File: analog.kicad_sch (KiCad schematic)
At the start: 45 parts, among them J8 Sensor harness

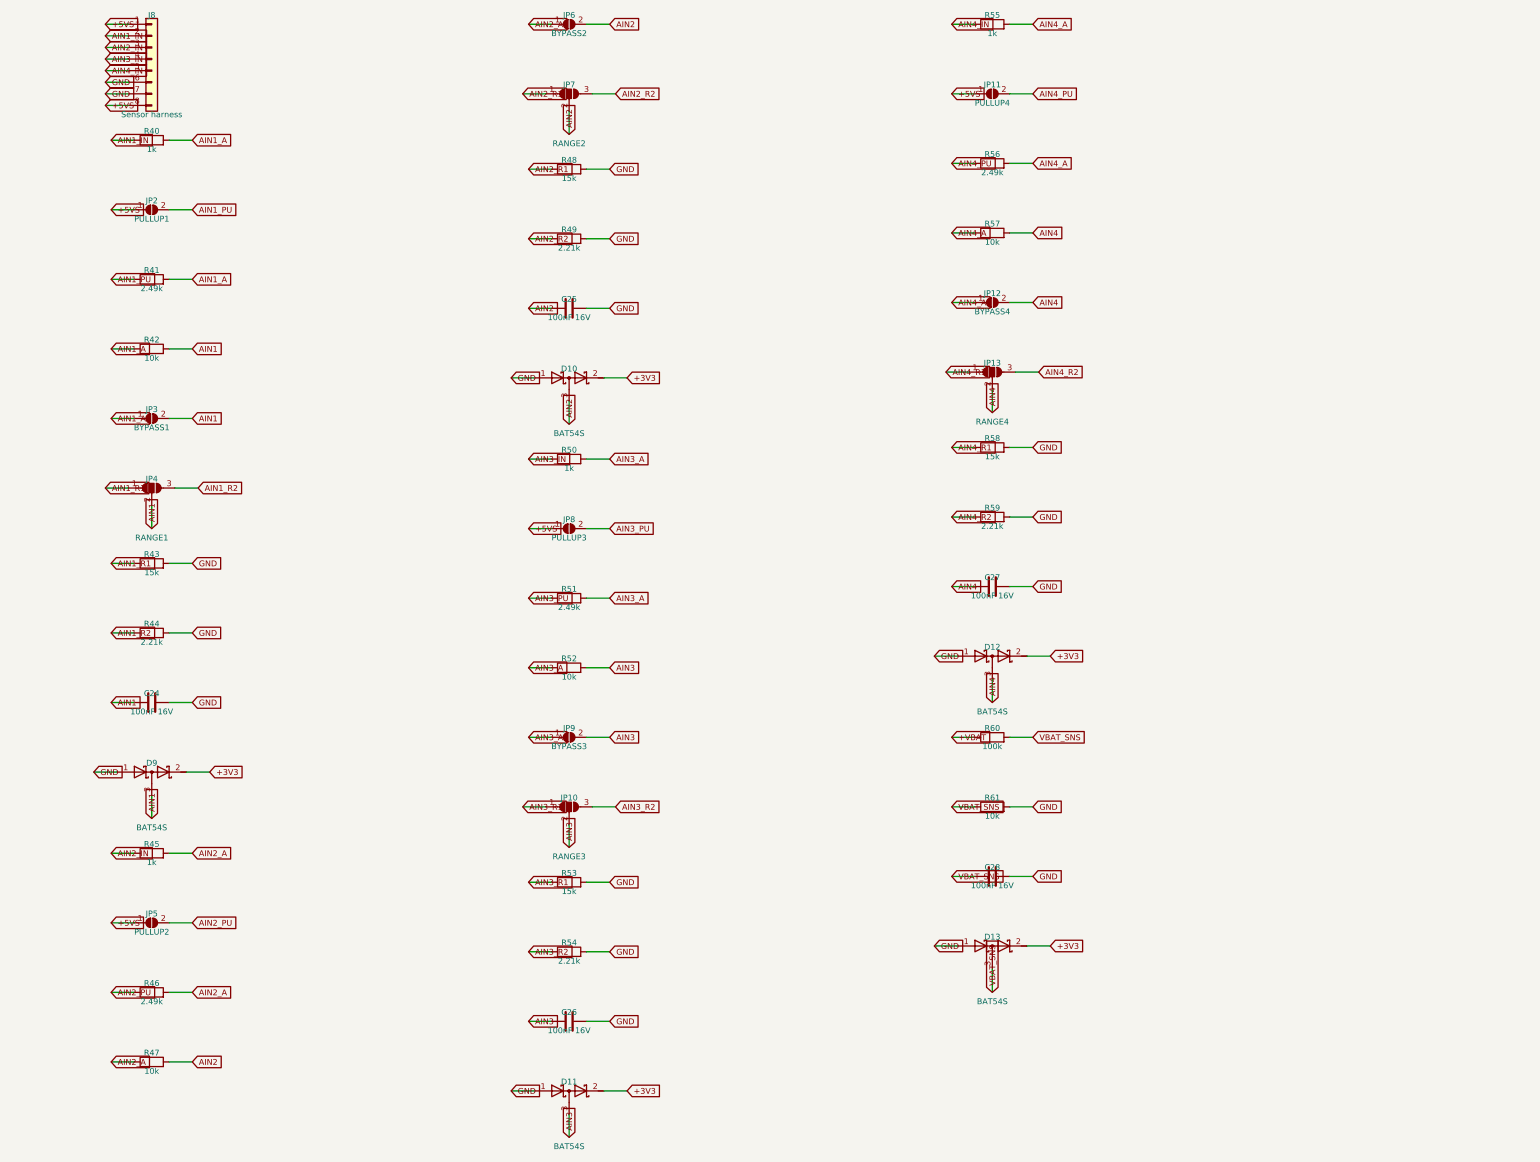
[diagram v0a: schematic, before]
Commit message: Pass ERC clean on KiCad 9.0 and regenerate against its libraries
- Add a PWR_FLAG on VBAT_FB so the LM74700 ANODE power-input pin, fed
  through the reverse-battery FET and EMI bead, no longer trips
  power_pin_not_driven.
- Resolve the generic MOSFET symbols from Transistor_FET where the
  KiCad 9 libraries moved them out of Device.
- Handle the KiCad 9 library format in the raw-symbol extractor: tab
  indentation, CRLF line endings, and no trailing space after the
  symbol name.
- Flatten derived symbols the way KiCad does — carry the child's whole
  property blocks into the parent geometry instead of only swapping the
  value strings — so the embedded USBLC6-2SC6 matches the library copy.
- Regenerate all sheets, netlist, and the PDF plot; embedded symbol
  definitions now come from the KiCad 9.0 (20241209) libraries.

Validated with kicad-cli 9.0: all sheets load, connectivity matches
netlist.txt on 102 nets / 153 instances, ERC clean.

Co-Authored-By: Claude Fable 5 <noreply@anthropic.com>
Claude-Session: https://claude.ai/code/session_01DhNbL25h25p8VFCjRfJik9
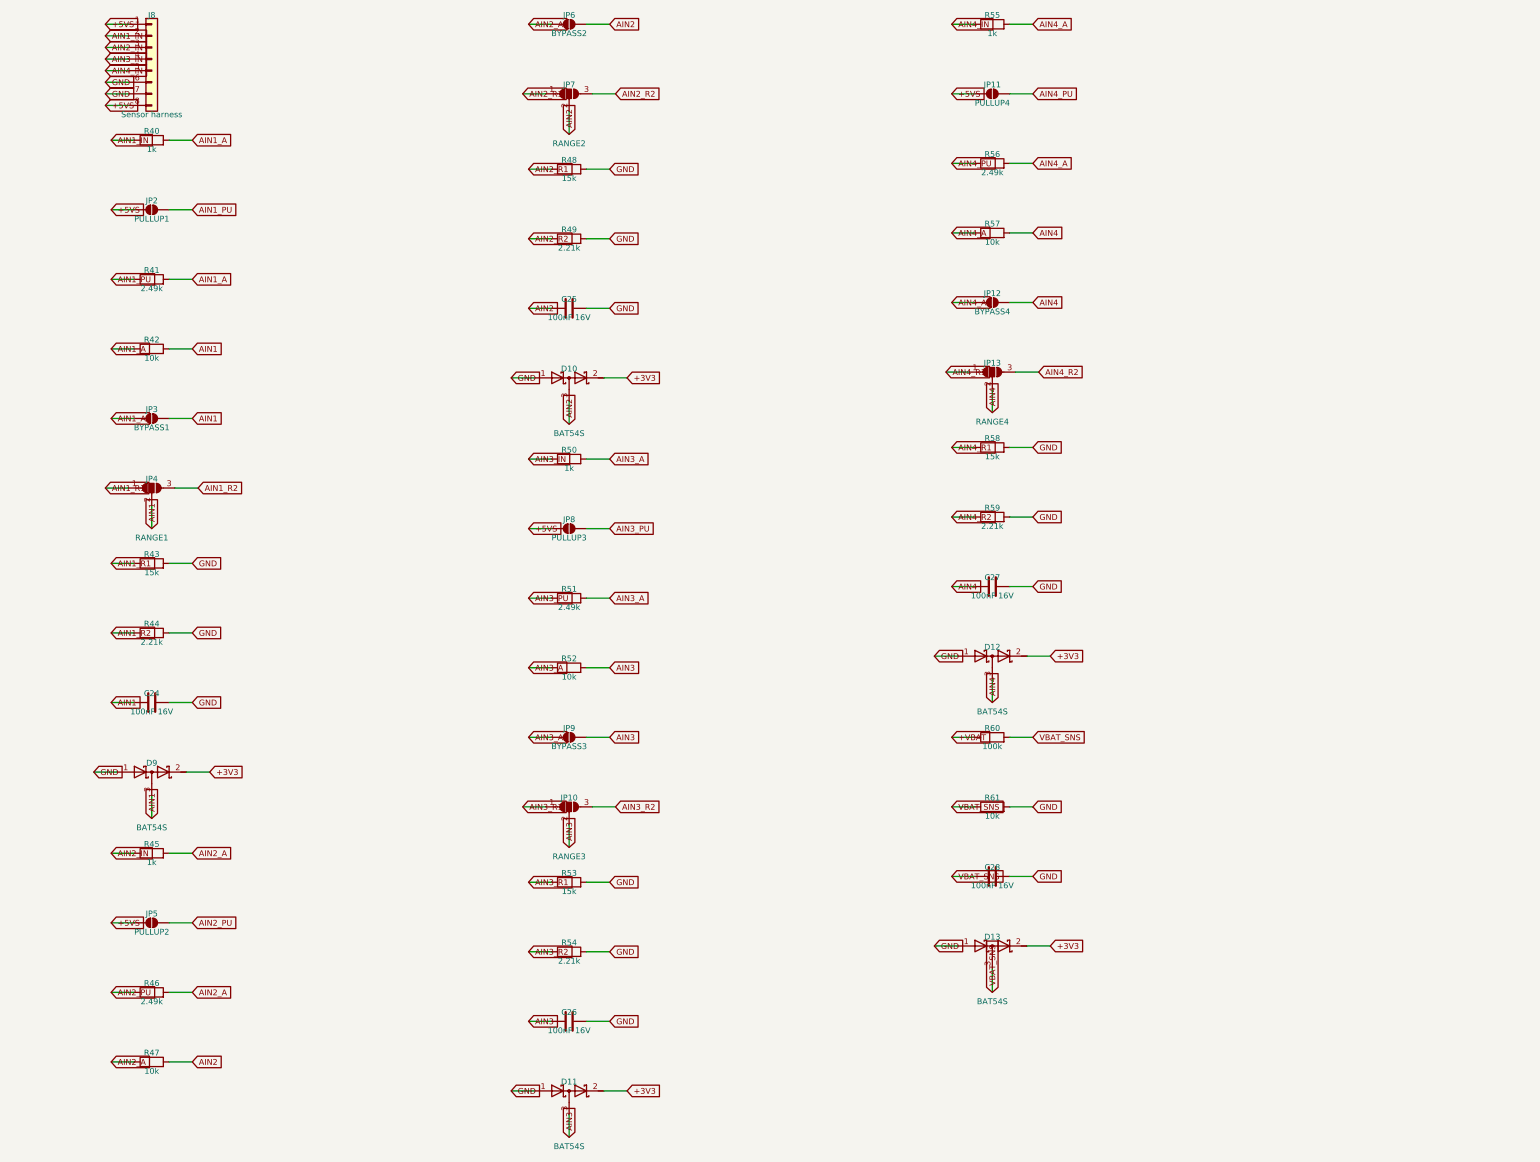
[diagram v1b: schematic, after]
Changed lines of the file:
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@@
+    (stroke (width 0) (type default))
+  )
+  (wire (pts (xy 54.61 186.69) (xy 54.61 191.77))
     (stroke (width 0) (type default))
   )
@@
     (stroke (width 0) (type default))
   )
-  (wire (pts (xy 54.61 186.69) (xy 54.61 191.77))
-    (stroke (width 0) (type default))
-  )
   (wire (pts (xy 50.8 199.39) (xy 45.72 199.39))
     (stroke (width 0) (type default))
@@
     (stroke (width 0) (type default))
   )
+  (wire (pts (xy 146.05 100.33) (xy 146.05 105.41))
+    (stroke (width 0) (type default))
+  )
   (wire (pts (xy 153.67 95.25) (xy 158.75 95.25))
     (stroke (width 0) (type default))
   )
-  (wire (pts (xy 146.05 100.33) (xy 146.05 105.41))
-    (stroke (width 0) (type default))
-  )
   (wire (pts (xy 142.24 113.03) (xy 137.16 113.03))
     (stroke (width 0) (type default))
@@
     (stroke (width 0) (type default))
   )
+  (wire (pts (xy 146.05 256.54) (xy 146.05 261.62))
+    (stroke (width 0) (type default))
+  )
   (wire (pts (xy 153.67 251.46) (xy 158.75 251.46))
     (stroke (width 0) (type default))
   )
-  (wire (pts (xy 146.05 256.54) (xy 146.05 261.62))
-    (stroke (width 0) (type default))
-  )
   (wire (pts (xy 234.95 17.78) (xy 229.87 17.78))
     (stroke (width 0) (type default))
@@
     (stroke (width 0) (type default))
   )
+  (wire (pts (xy 238.76 161.29) (xy 238.76 166.37))
+    (stroke (width 0) (type default))
+  )
   (wire (pts (xy 246.38 156.21) (xy 251.46 156.21))
     (stroke (width 0) (type default))
   )
-  (wire (pts (xy 238.76 161.29) (xy 238.76 166.37))
-    (stroke (width 0) (type default))
-  )
   (wire (pts (xy 234.95 173.99) (xy 229.87 173.99))
     (stroke (width 0) (type default))
@@
     (stroke (width 0) (type default))
   )
+  (wire (pts (xy 238.76 224.79) (xy 238.76 229.87))
+    (stroke (width 0) (type default))
+  )
   (wire (pts (xy 246.38 219.71) (xy 251.46 219.71))
     (stroke (width 0) (type default))
   )
-  (wire (pts (xy 238.76 224.79) (xy 238.76 229.87))
-    (stroke (width 0) (type default))
-  )
   (global_label "+5VS" (shape input) (at 44.45 17.78 180) (fields_autoplaced)
     (effects (font (size 1.27 1.27)) (justify left))
@@
     )
   )
+  (global_label "AIN1" (shape input) (at 54.61 191.77 270) (fields_autoplaced)
+    (effects (font (size 1.27 1.27)) (justify left))
+    (property "Intersheet References" "${INTERSHEET_REFS}" (at 54.61 191.77 0)
+      (effects (font (size 1.27 1.27)) (justify left) hide)
+    )
+  )
   (global_label "+3V3" (shape input) (at 67.31 181.61 0) (fields_autoplaced)
     (effects (font (size 1.27 1.27)) (justify left))
@@
     )
   )
-  (global_label "AIN1" (shape input) (at 54.61 191.77 270) (fields_autoplaced)
-    (effects (font (size 1.27 1.27)) (justify left))
-    (property "Intersheet References" "${INTERSHEET_REFS}" (at 54.61 191.77 0)
-      (effects (font (size 1.27 1.27)) (justify left) hide)
-    )
-  )
   (global_label "AIN2_IN" (shape input) (at 45.72 199.39 180) (fields_autoplaced)
     (effects (font (size 1.27 1.27)) (justify left))
@@
     )
   )
+  (global_label "AIN2" (shape input) (at 146.05 105.41 270) (fields_autoplaced)
+    (effects (font (size 1.27 1.27)) (justify left))
+    (property "Intersheet References" "${INTERSHEET_REFS}" (at 146.05 105.41 0)
+      (effects (font (size 1.27 1.27)) (justify left) hide)
+    )
+  )
   (global_label "+3V3" (shape input) (at 158.75 95.25 0) (fields_autoplaced)
     (effects (font (size 1.27 1.27)) (justify left))
@@
     )
   )
-  (global_label "AIN2" (shape input) (at 146.05 105.41 270) (fields_autoplaced)
-    (effects (font (size 1.27 1.27)) (justify left))
-    (property "Intersheet References" "${INTERSHEET_REFS}" (at 146.05 105.41 0)
-      (effects (font (size 1.27 1.27)) (justify left) hide)
-    )
-  )
   (global_label "AIN3_IN" (shape input) (at 137.16 113.03 180) (fields_autoplaced)
     (effects (font (size 1.27 1.27)) (justify left))
@@
     )
   )
+  (global_label "AIN3" (shape input) (at 146.05 261.62 270) (fields_autoplaced)
+    (effects (font (size 1.27 1.27)) (justify left))
+    (property "Intersheet References" "${INTERSHEET_REFS}" (at 146.05 261.62 0)
+      (effects (font (size 1.27 1.27)) (justify left) hide)
+    )
+  )
   (global_label "+3V3" (shape input) (at 158.75 251.46 0) (fields_autoplaced)
     (effects (font (size 1.27 1.27)) (justify left))
@@
     )
   )
-  (global_label "AIN3" (shape input) (at 146.05 261.62 270) (fields_autoplaced)
-    (effects (font (size 1.27 1.27)) (justify left))
-    (property "Intersheet References" "${INTERSHEET_REFS}" (at 146.05 261.62 0)
-      (effects (font (size 1.27 1.27)) (justify left) hide)
-    )
-  )
   (global_label "AIN4_IN" (shape input) (at 229.87 17.78 180) (fields_autoplaced)
     (effects (font (size 1.27 1.27)) (justify left))
@@
     )
   )
+  (global_label "AIN4" (shape input) (at 238.76 166.37 270) (fields_autoplaced)
+    (effects (font (size 1.27 1.27)) (justify left))
+    (property "Intersheet References" "${INTERSHEET_REFS}" (at 238.76 166.37 0)
+      (effects (font (size 1.27 1.27)) (justify left) hide)
+    )
+  )
   (global_label "+3V3" (shape input) (at 251.46 156.21 0) (fields_autoplaced)
     (effects (font (size 1.27 1.27)) (justify left))
@@
     )
   )
-  (global_label "AIN4" (shape input) (at 238.76 166.37 270) (fields_autoplaced)
-    (effects (font (size 1.27 1.27)) (justify left))
-    (property "Intersheet References" "${INTERSHEET_REFS}" (at 238.76 166.37 0)
-      (effects (font (size 1.27 1.27)) (justify left) hide)
-    )
-  )
   (global_label "+VBAT" (shape input) (at 229.87 173.99 180) (fields_autoplaced)
     (effects (font (size 1.27 1.27)) (justify left))
@@
     )
   )
+  (global_label "VBAT_SNS" (shape input) (at 238.76 229.87 270) (fields_autoplaced)
+    (effects (font (size 1.27 1.27)) (justify left))
+    (property "Intersheet References" "${INTERSHEET_REFS}" (at 238.76 229.87 0)
+      (effects (font (size 1.27 1.27)) (justify left) hide)
+    )
+  )
   (global_label "+3V3" (shape input) (at 251.46 219.71 0) (fields_autoplaced)
     (effects (font (size 1.27 1.27)) (justify left))
     (property "Intersheet References" "${INTERSHEET_REFS}" (at 251.46 219.71 0)
-      (effects (font (size 1.27 1.27)) (justify left) hide)
-    )
-  )
-  (global_label "VBAT_SNS" (shape input) (at 238.76 229.87 270) (fields_autoplaced)
-    (effects (font (size 1.27 1.27)) (justify left))
-    (property "Intersheet References" "${INTERSHEET_REFS}" (at 238.76 229.87 0)
       (effects (font (size 1.27 1.27)) (justify left) hide)
     )
@@
     )
     (pin "1")
-    (pin "2")
     (pin "3")
+    (pin "2")
     (instances
       (project "esp32s3-can-sd-logger"
@@
     )
     (pin "1")
-    (pin "2")
     (pin "3")
+    (pin "2")
     (instances
       (project "esp32s3-can-sd-logger"
@@
     )
     (pin "1")
-    (pin "2")
     (pin "3")
+    (pin "2")
     (instances
       (project "esp32s3-can-sd-logger"
@@
     )
     (pin "1")
-    (pin "2")
     (pin "3")
+    (pin "2")
     (instances
       (project "esp32s3-can-sd-logger"
@@
     )
     (pin "1")
-    (pin "2")
     (pin "3")
-    (instances
-      (project "esp32s3-can-sd-logger"
+    (pin "2")
+    (instances
+      (project "esp32s3-can-sd-logger"
